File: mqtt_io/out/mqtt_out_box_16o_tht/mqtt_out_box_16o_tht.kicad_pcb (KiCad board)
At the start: 2 copper layers, 125.9 x 182.5 mm, 106 parts, among them J1 Conn_01x04_Pin, J18 Conn_01x04_Pin, K1 FINDER-40.31, K10 FINDER-40.31, K11 FINDER-40.31, K12 FINDER-40.31, K13 FINDER-40.31, K14 FINDER-40.31, K15 FINDER-40.31, K16 FINDER-40.31, K2 FINDER-40.31, K3 FINDER-40.31, K4 FINDER-40.31, K5 FINDER-40.31, K6 FINDER-40.31, K7 FINDER-40.31, K8 FINDER-40.31, K9 FINDER-40.31, Q1 IRFZ24N, Q10 IRFZ24N, Q11 IRFZ24N, Q12 IRFZ24N, Q13 IRFZ24N, Q14 IRFZ24N, Q15 IRFZ24N, Q16 IRFZ24N, Q2 IRFZ24N, Q3 IRFZ24N, Q4 IRFZ24N, Q5 IRFZ24N, Q6 IRFZ24N, Q7 IRFZ24N, Q8 IRFZ24N, Q9 IRFZ24N, U1 MCP23017_SP

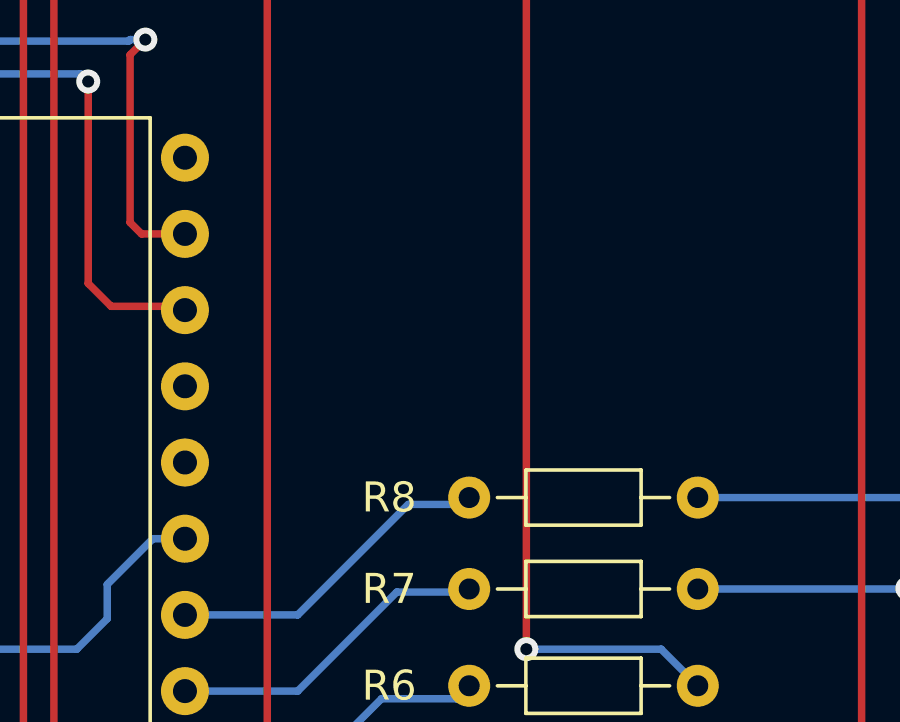
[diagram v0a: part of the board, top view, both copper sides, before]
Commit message: Pullup für ic2 eingefügt (4k7)
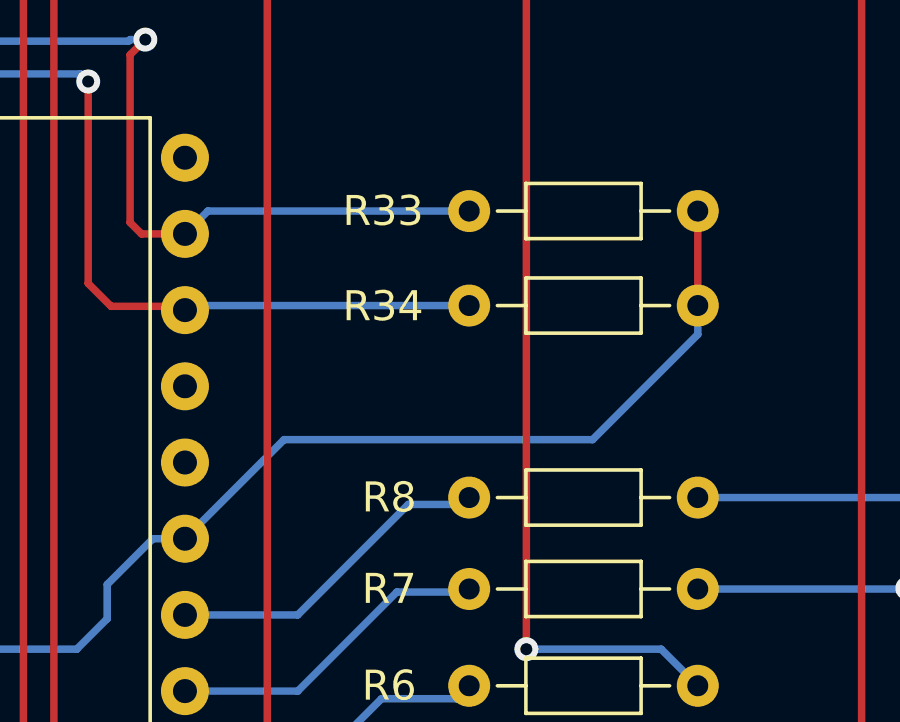
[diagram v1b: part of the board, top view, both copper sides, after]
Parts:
- added R33: 4k7, Resistor_THT:R_Axial_DIN0204_L3.6mm_D1.6mm_P7.62mm_Horizontal, F.Cu at (95.1, 150.5)
- added R34: 4k7, Resistor_THT:R_Axial_DIN0204_L3.6mm_D1.6mm_P7.62mm_Horizontal, F.Cu at (95.1, 153.6)
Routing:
- net VCC: track 494.6 -> 518.6 mm
- net Net-(J1-Pin_2): track 88.7 -> 98.5 mm
- net Net-(J1-Pin_3): track 88.4 -> 97.9 mm
